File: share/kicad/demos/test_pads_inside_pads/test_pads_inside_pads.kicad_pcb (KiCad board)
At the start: 2 copper layers, 4 parts, among them P1 CONN_1, P2 CONN_1, P3 CONN_1, P4 CONN_1

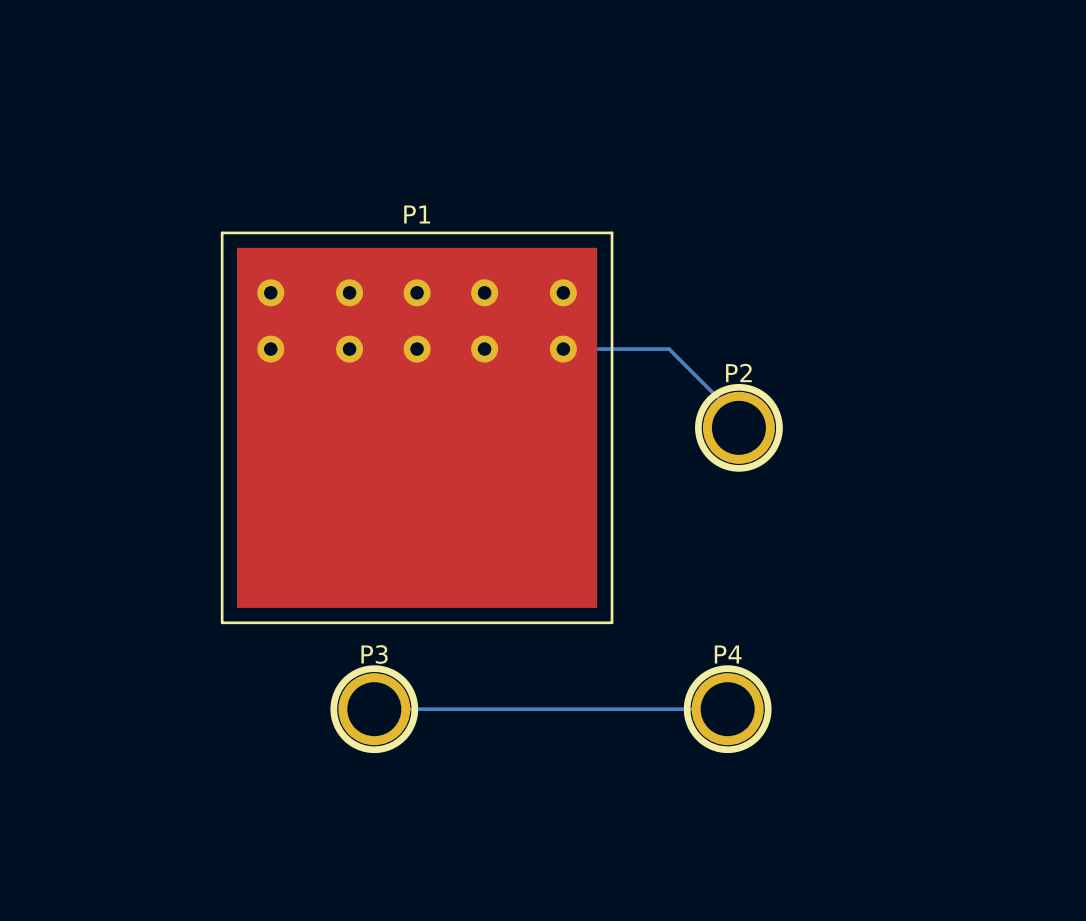
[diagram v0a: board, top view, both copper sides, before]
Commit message: Remove KiCad V4.0.7
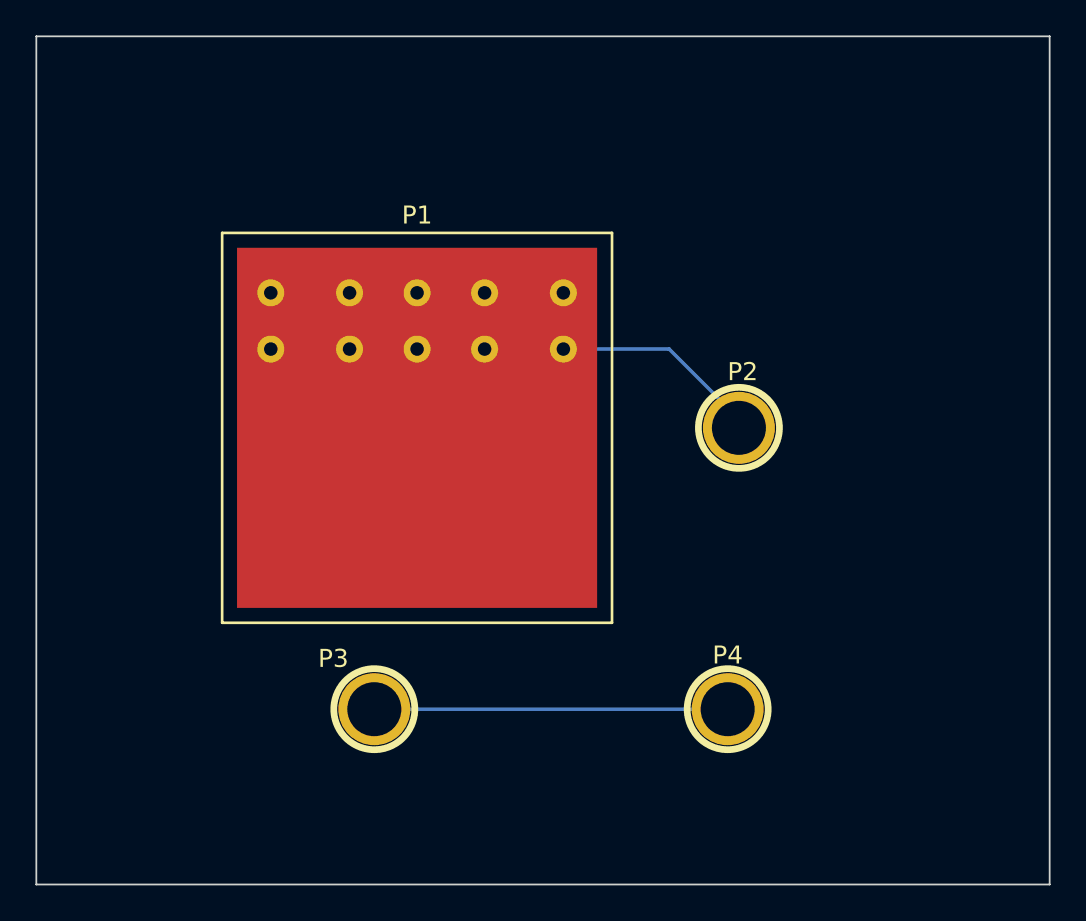
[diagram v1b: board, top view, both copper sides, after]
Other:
- board outline added: 57.2 x 47.9 mm
- net class Default removed
- rule pad_to_mask_clearance: 0.254 -> 0
